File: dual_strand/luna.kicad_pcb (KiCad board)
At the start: 2 copper layers, 26 x 44 mm, 23 parts, among them J1 Conn_01x06_MountingPin, J2 Conn_01x01, J3 Conn_01x01, Q1 DMN3404L, Q2 DMN3404L, Q3 DMN3404L, Q4 DMN3404L, U1 AP65211AWU, U2 ESP32-WROOM-32, U3 TSOP343xx

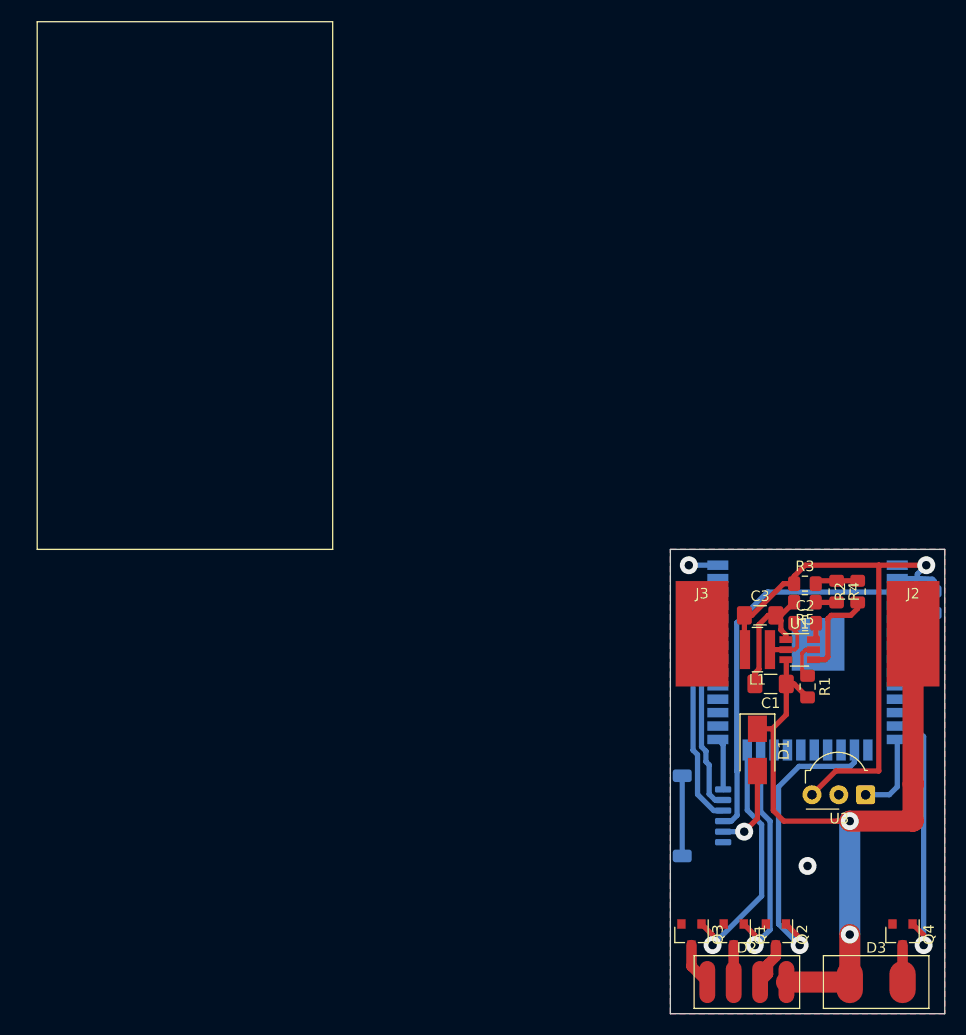
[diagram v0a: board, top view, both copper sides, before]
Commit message: Added MOSFET pull-downs. Moved IR receiver to the other side. Shrunk ground plane
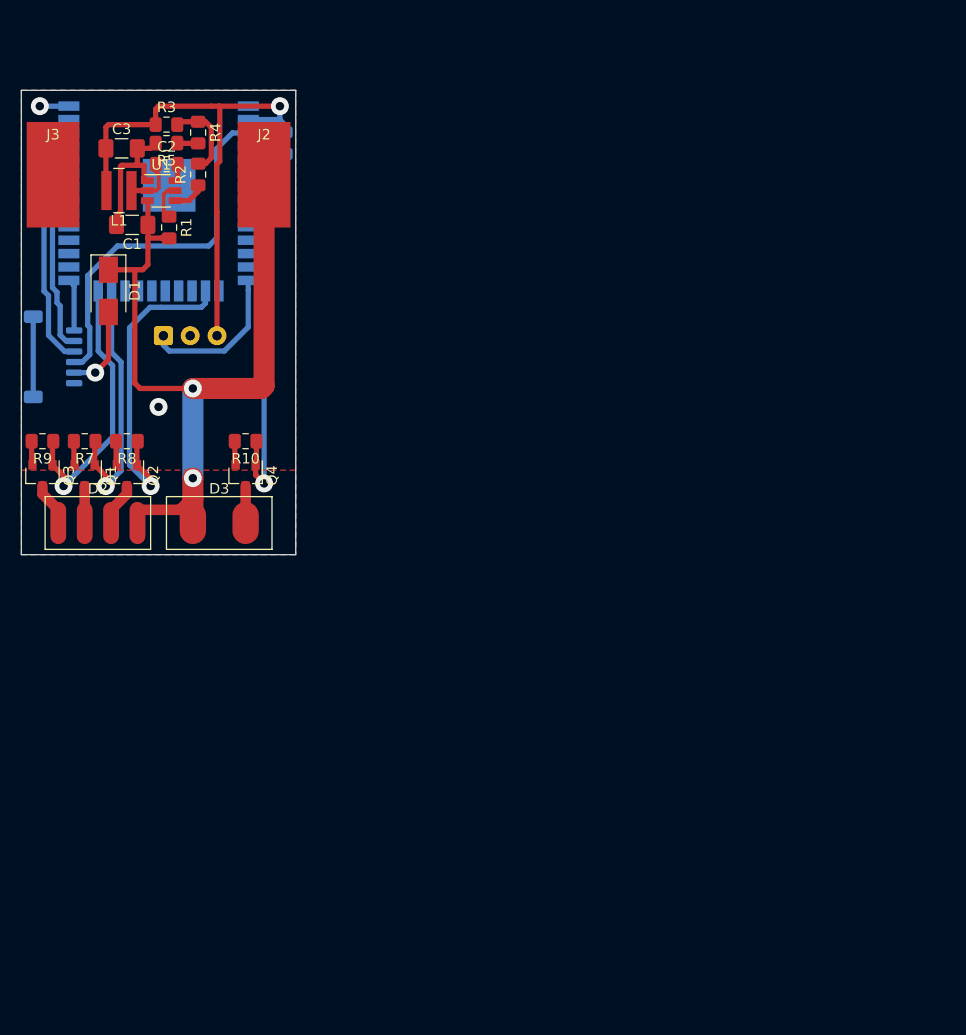
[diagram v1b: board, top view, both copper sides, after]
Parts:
- added R10: 1k, Resistor_SMD:R_0805_2012Metric_Pad1.15x1.40mm_HandSolder, F.Cu at (39.8, 59.8)
- added R7: 1k, Resistor_SMD:R_0805_2012Metric_Pad1.15x1.40mm_HandSolder, F.Cu at (24.5, 59.8)
- added R8: 1k, Resistor_SMD:R_0805_2012Metric_Pad1.15x1.40mm_HandSolder, F.Cu at (28.5, 59.8)
- added R9: 1k, Resistor_SMD:R_0805_2012Metric_Pad1.15x1.40mm_HandSolder, F.Cu at (20.5, 59.8)
- U3: moved to B.Cu
- moved U3 79.5 mm to (32.0, 49.8), turned to 0 degrees
- moved D3 75.9 mm to (37.2, 67.5)
- moved Q4 75.9 mm to (39.8, 63.0)
- moved D1 75.3 mm to (26.8, 45.5)
- moved D2 75.3 mm to (25.8, 67.5)
- moved J1 75.3 mm to (21.5, 51.8)
- moved J2 75.3 mm to (41.5, 34.5)
- moved J3 75.3 mm to (21.5, 34.5)
- moved Q1 75.3 mm to (24.5, 63.0)
- moved Q2 75.3 mm to (28.5, 63.0)
- moved Q3 75.3 mm to (20.5, 63.0)
- moved R6 75.3 mm to (43.5, 31.5)
- moved U2 75.3 mm to (31.5, 36.3)
- moved C3 75.0 mm to (28.0, 32.0)
- moved C2 74.5 mm to (32.3, 33.5)
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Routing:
- net GND: track 23.0 -> 32.6 mm
- net IR: track 7.80 -> 14.5 mm
- net Net-(R2-Pad1): track 8.89 -> 3.13 mm
- net VDD: track 56.0 -> 51.0 mm
- net Net-(R2-Pad2): track 4.09 -> 7.92 mm
- net +12V: track 71.5 -> 75.0 mm
- net LED_G: track 27.7 -> 30.0 mm
- net LED_R: track 21.9 -> 24.2 mm
- net LED_B: track 23.4 -> 25.7 mm
- net LED_W: track 25.1 -> 26.4 mm
- net EN: track 40.6 -> 39.4 mm
